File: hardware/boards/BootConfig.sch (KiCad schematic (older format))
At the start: 33 parts, among them J3 Conn_02x05_Odd_Even, Q6 Q_NMOS_GSD, SW1 SW_DIP_x03, SW2 RESET, U1 ECP5UM5G-381caBGA, U3 CYUSB3014, U5 128MiB

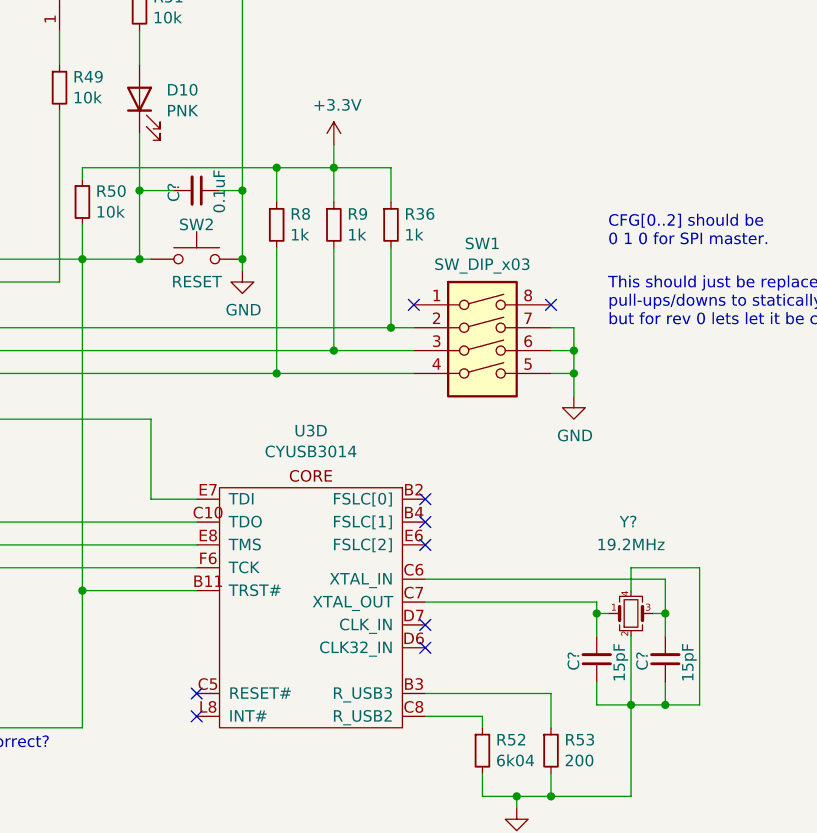
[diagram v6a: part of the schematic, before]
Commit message: Annotated the schematics and updated the PCB with the new imported parts
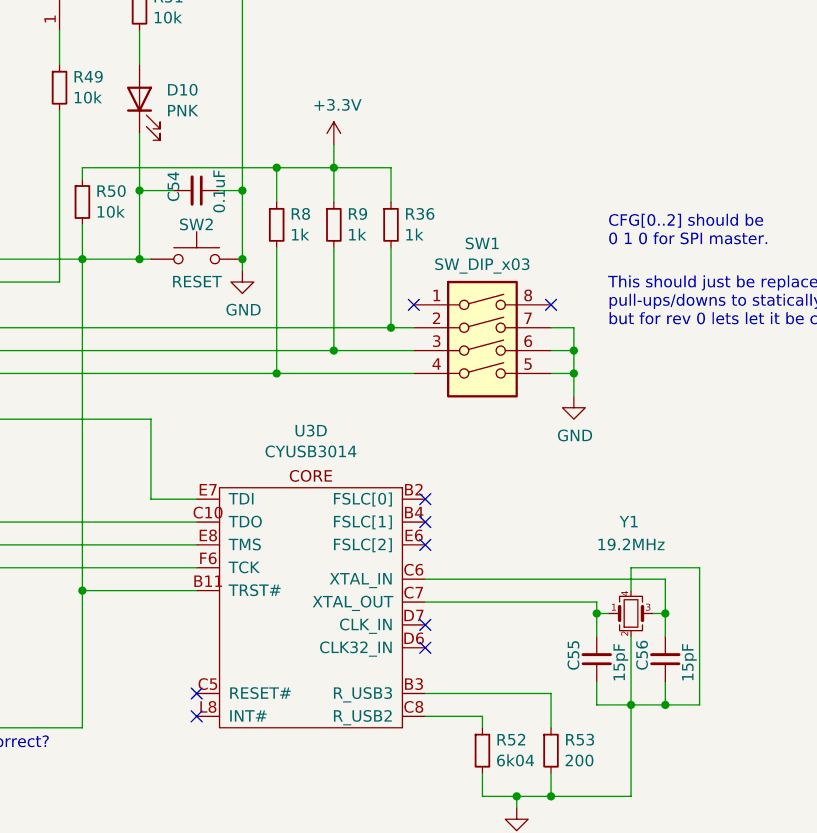
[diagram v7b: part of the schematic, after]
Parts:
- gave numbers to parts that had none: 4
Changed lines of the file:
@@
 P 8950 4350
 AR Path="/5EDF9F51/606E230C" Ref="C?"  Part="1"
-AR Path="/5EF66251/606E230C" Ref="C?"  Part="1"
-F 0 "C?" H 9000 4250 50  0000 R CNN
+AR Path="/5EF66251/606E230C" Ref="C54"  Part="1"
+F 0 "C54" H 9000 4250 50  0000 R CNN
 F 1 "0.1uF" H 9050 4450 50  0000 R CNN
 F 2 "Capacitor_SMD:C_0603_1608Metric" H 8950 4350 50  0001 C CNN
@@
 	9150 4350 9150 4650
 $Comp
-L Device:Crystal_GND24_Small Y?
+L Device:Crystal_GND24_Small Y1
 U 1 1 6071D344
 P 10850 6200
-F 0 "Y?" H 10800 6600 50  0000 L CNN
+F 0 "Y1" H 10800 6600 50  0000 L CNN
 F 1 "19.2MHz" H 10700 6500 50  0000 L CNN
 F 2 "Crystal:Crystal_SMD_Abracon_ABM10-4Pin_2.5x2.0mm" H 10850 6200 50  0001 C CNN
@@
 P 10700 6400
 AR Path="/5EDF9F51/60727D1B" Ref="C?"  Part="1"
-AR Path="/5EF66251/60727D1B" Ref="C?"  Part="1"
-F 0 "C?" V 10800 6450 50  0000 R CNN
+AR Path="/5EF66251/60727D1B" Ref="C55"  Part="1"
+F 0 "C55" V 10800 6450 50  0000 R CNN
 F 1 "15pF" V 10600 6500 50  0000 R CNN
 F 2 "Capacitor_SMD:C_0603_1608Metric" H 10700 6400 50  0001 C CNN
@@
 P 11000 6400
 AR Path="/5EDF9F51/607291D9" Ref="C?"  Part="1"
-AR Path="/5EF66251/607291D9" Ref="C?"  Part="1"
-F 0 "C?" V 11100 6450 50  0000 R CNN
+AR Path="/5EF66251/607291D9" Ref="C56"  Part="1"
+F 0 "C56" V 11100 6450 50  0000 R CNN
 F 1 "15pF" V 10900 6500 50  0000 R CNN
 F 2 "Capacitor_SMD:C_0603_1608Metric" H 11000 6400 50  0001 C CNN

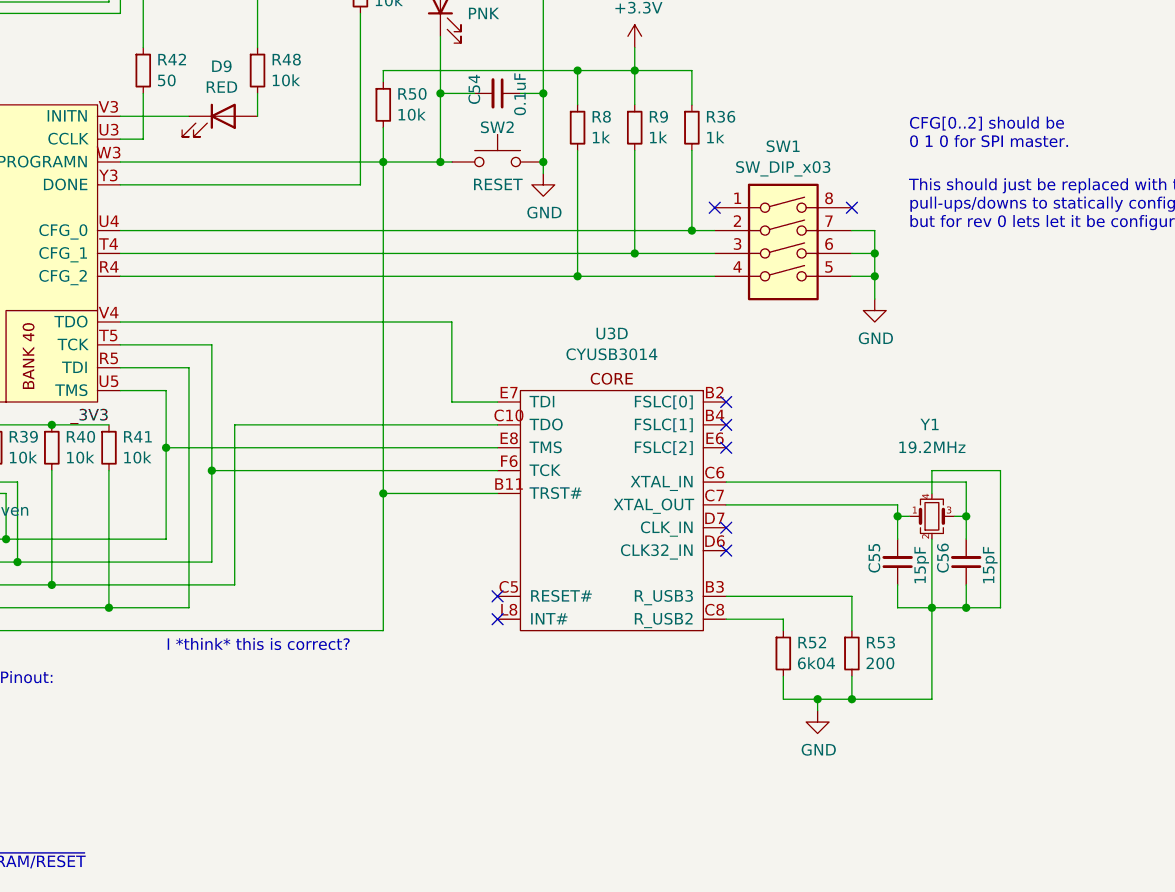
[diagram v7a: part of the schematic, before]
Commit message: Added the 3D model to the crystal
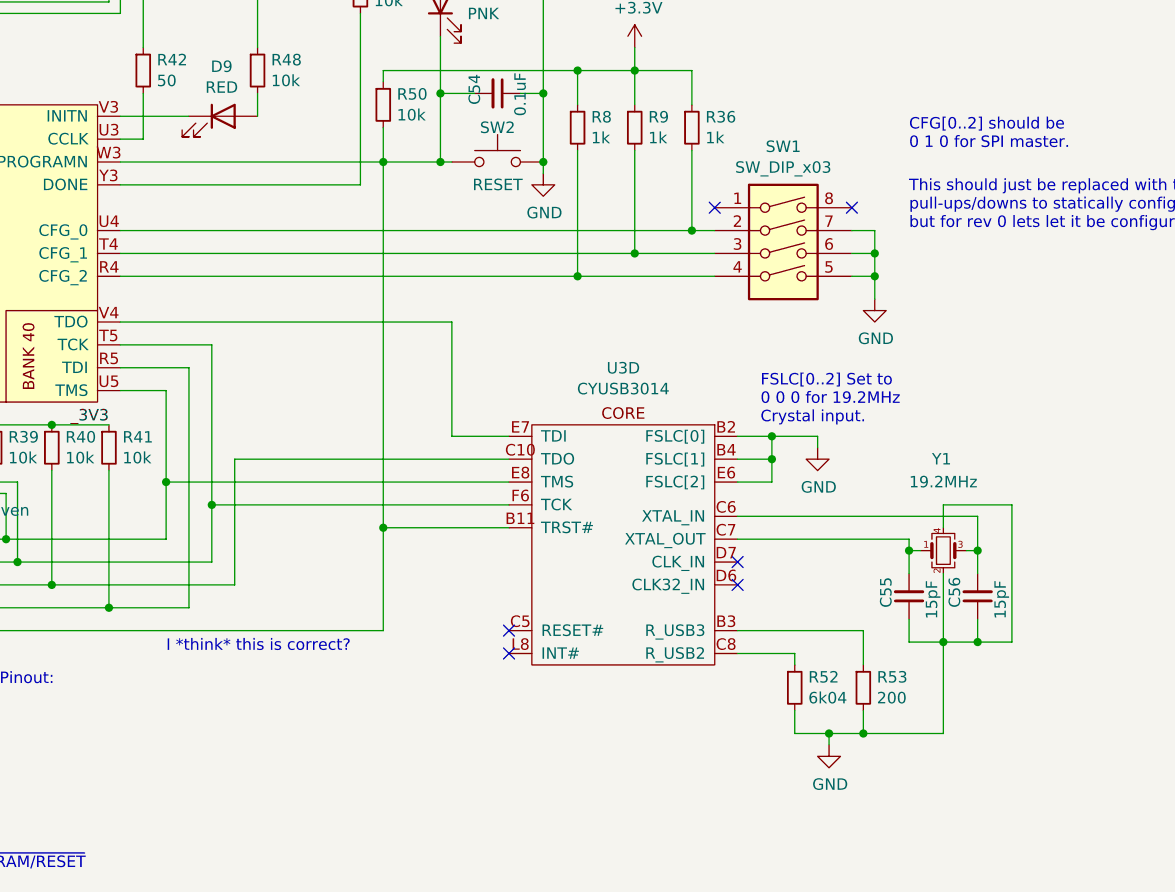
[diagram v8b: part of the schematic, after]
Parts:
- Y1: footprint Crystal:Crystal_SMD_Abracon_ABM10-4Pin_2.5x2.0mm -> lethalbit:Crystal_SMD_Abracon_ABM10-4Pin_2.5x2.0mm
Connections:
- net GND: now also U3.B2 (FSLC[0]), U3.B4 (FSLC[1]), U3.E6 (FSLC[2])
- no-connect marks 18 -> 15
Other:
- note added: "FSLC[0..2] Set to\n0 0 0 for 19.2MHz\nCrystal input.\n"
- moved on the sheet: C55, C56, R52, R53, U3D, Y1
